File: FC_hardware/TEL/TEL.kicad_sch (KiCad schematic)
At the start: 12 parts, among them J1 Conn_01x14, J2 Conn_01x01_Pin, U1 Ai-Thinker-Ra-02, U2 TESEO-LIV4F, U3 LIS3MDL

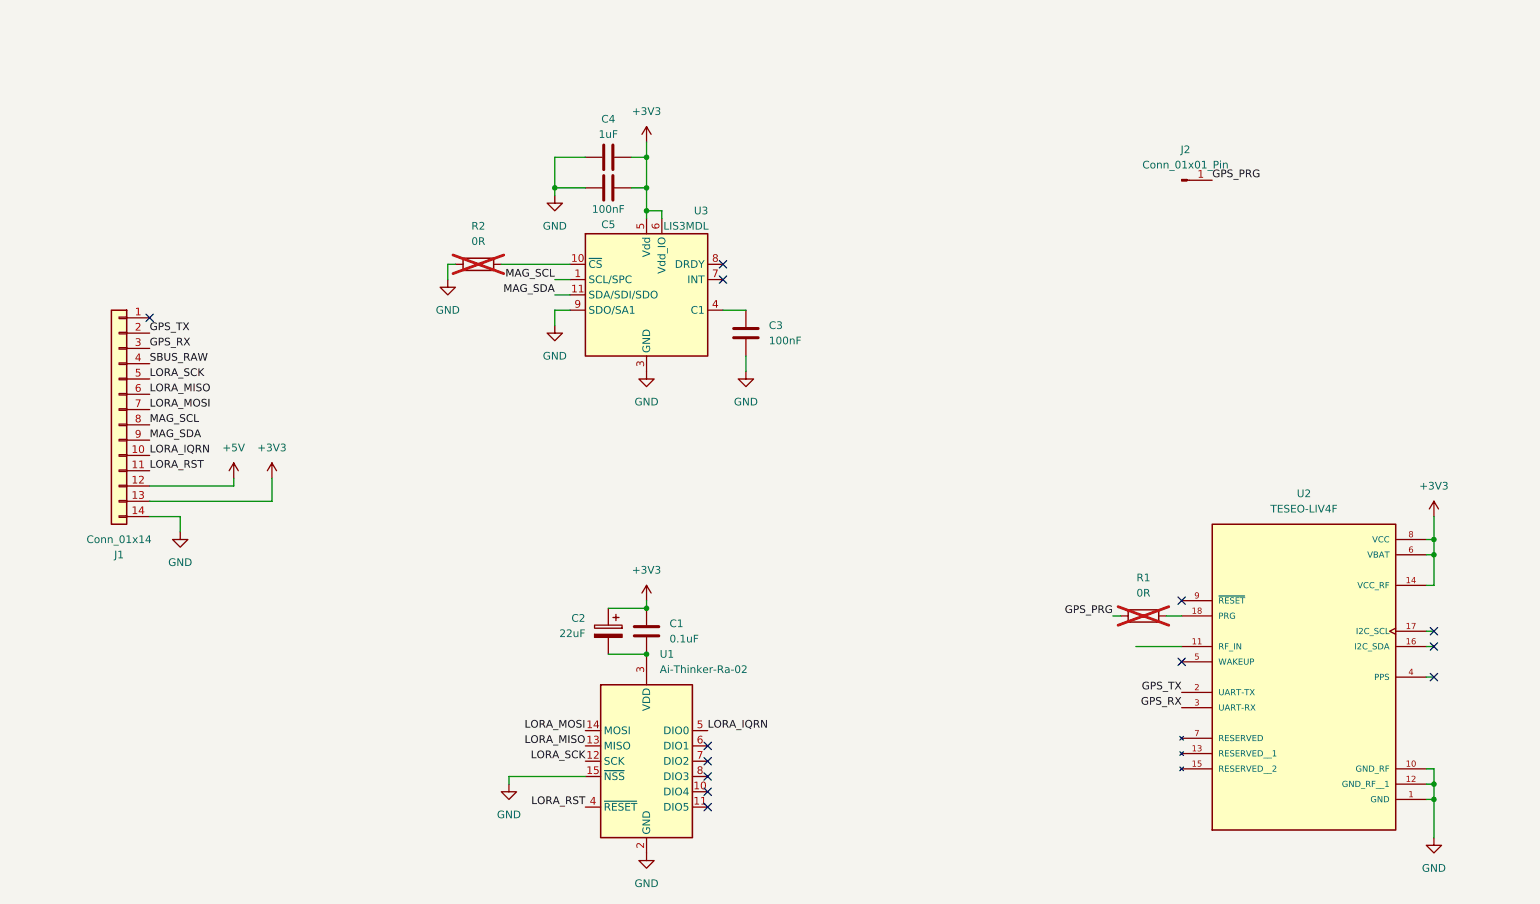
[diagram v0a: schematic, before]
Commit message: Set chip antenna footprint
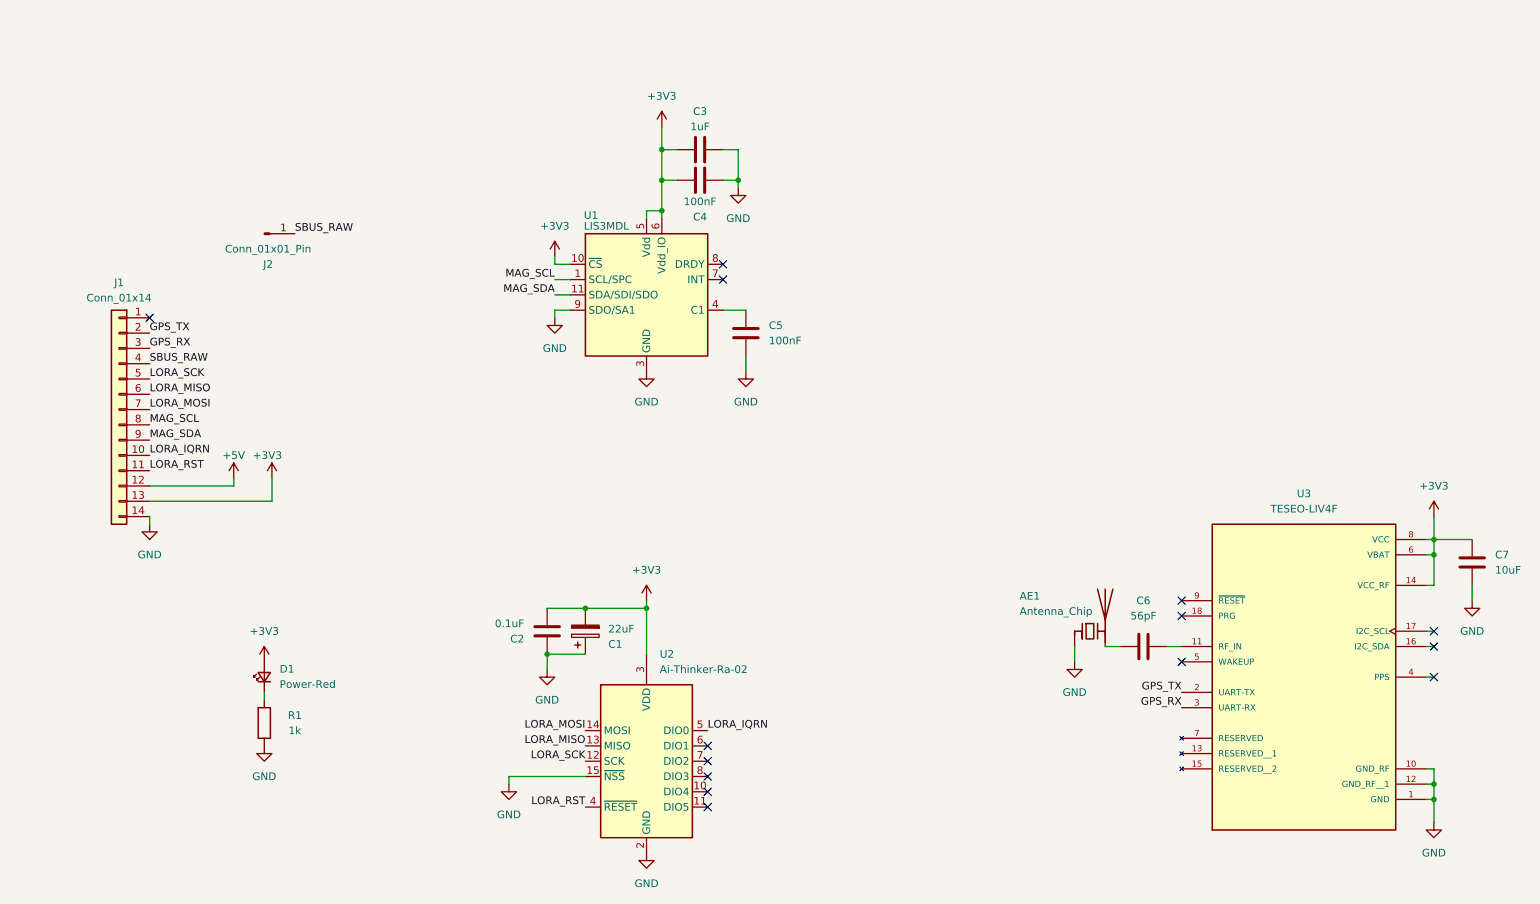
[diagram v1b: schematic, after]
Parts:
- removed R2: 0R, symbol Device:R
- removed U2: TESEO-LIV4F, TESEO-LIV4F:XCVR_TESEO-LIV4F, symbol gps:TESEO-LIV4F
- added AE1: Antenna_Chip, RF_Antenna:Pulse_W3011, symbol Device:Antenna_Chip
- added C6: 56pF, Capacitor_SMD:C_0402_1005Metric, symbol Device:C
- added C7: 10uF, Capacitor_SMD:C_0603_1608Metric, symbol Device:C
- added D1: Power-Red, LED_SMD:LED_0805_2012Metric, symbol Device:LED_Small
- added U3: TESEO-LIV4F, gps:XCVR_TESEO-LIV4F, symbol gps:TESEO-LIV4F
- C1: renamed from C2; footprint (none) -> Capacitor_Tantalum_SMD:CP_EIA-3528-12_Kemet-T
- C2: renamed from C1; footprint (none) -> Capacitor_SMD:C_0603_1608Metric
- C3: renamed from C4; footprint (none) -> Capacitor_SMD:C_0603_1608Metric
- C4: renamed from C5; footprint (none) -> Capacitor_SMD:C_0603_1608Metric
- C5: renamed from C3; footprint (none) -> Capacitor_SMD:C_0603_1608Metric
- J2: footprint (none) -> Connector_PinHeader_1.27mm:PinHeader_1x01_P1.27mm_Vertical
- R1: value 0R -> 1k; footprint (none) -> Resistor_SMD:R_0603_1608Metric; now fitted
- renumbered U3 to U1, U1 to U2
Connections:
- net +3V3: now also C1.2, C2.2, U1.10 (~{CS}), U2.3 (VDD), C7.1, D1.2 (A), U3.14 (VCC_RF), U3.6 (VBAT), U3.8 (VCC); no longer C1.1, C2.1
- net GND: now also C1.1, C2.1, R1.1, AE1.1 (FEED), C7.2, U3.1 (GND), U3.10 (GND_RF), U3.12 (GND_RF__1)
- net GPS_RX: now also U3.3 (UART-RX)
- net GPS_TX: now also U3.2 (UART-TX)
- net SBUS_RAW: now also J2.1 (Pin_1)
- net at R1.2: now also D1.1 (K)
- removed net GPS_PRG: J2.1 (Pin_1), R1.1
- new net: AE1.2 (PCB_Trace), C6.2
- new net: C6.1, U3.11 (RF_IN)
- no-connect marks 13 -> 14
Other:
- moved on the sheet: C1, C2, C3, C4

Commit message: Clean up
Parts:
- removed J2: Conn_01x01_Pin, Connector_PinHeader_1.27mm:PinHeader_1x01_P1.27mm_Vertical, symbol Connector:Conn_01x01_Pin
- added L1: L, symbol Device:L
- AE1: value Antenna_Chip -> W3011
- C6: value 56pF -> C
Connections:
- net GND: now also C6.2
- net at AE1.2 (PCB_Trace): now also C6.1, L1.1; no longer C6.2
- net GPS_ANT: now reaches U3.11 (RF_IN)
- net GPS_ANT: now also L1.2; no longer C6.1
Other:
- note added: "Antenna"
- note added: "GPS"
- note added: "LORA"
- note added: "Magnetometer"
- moved on the sheet: AE1, C1, C2, C3, C4, C5, C6, C7, D1, J1, R1, U1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
